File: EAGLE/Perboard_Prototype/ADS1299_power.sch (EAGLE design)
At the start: 24 parts

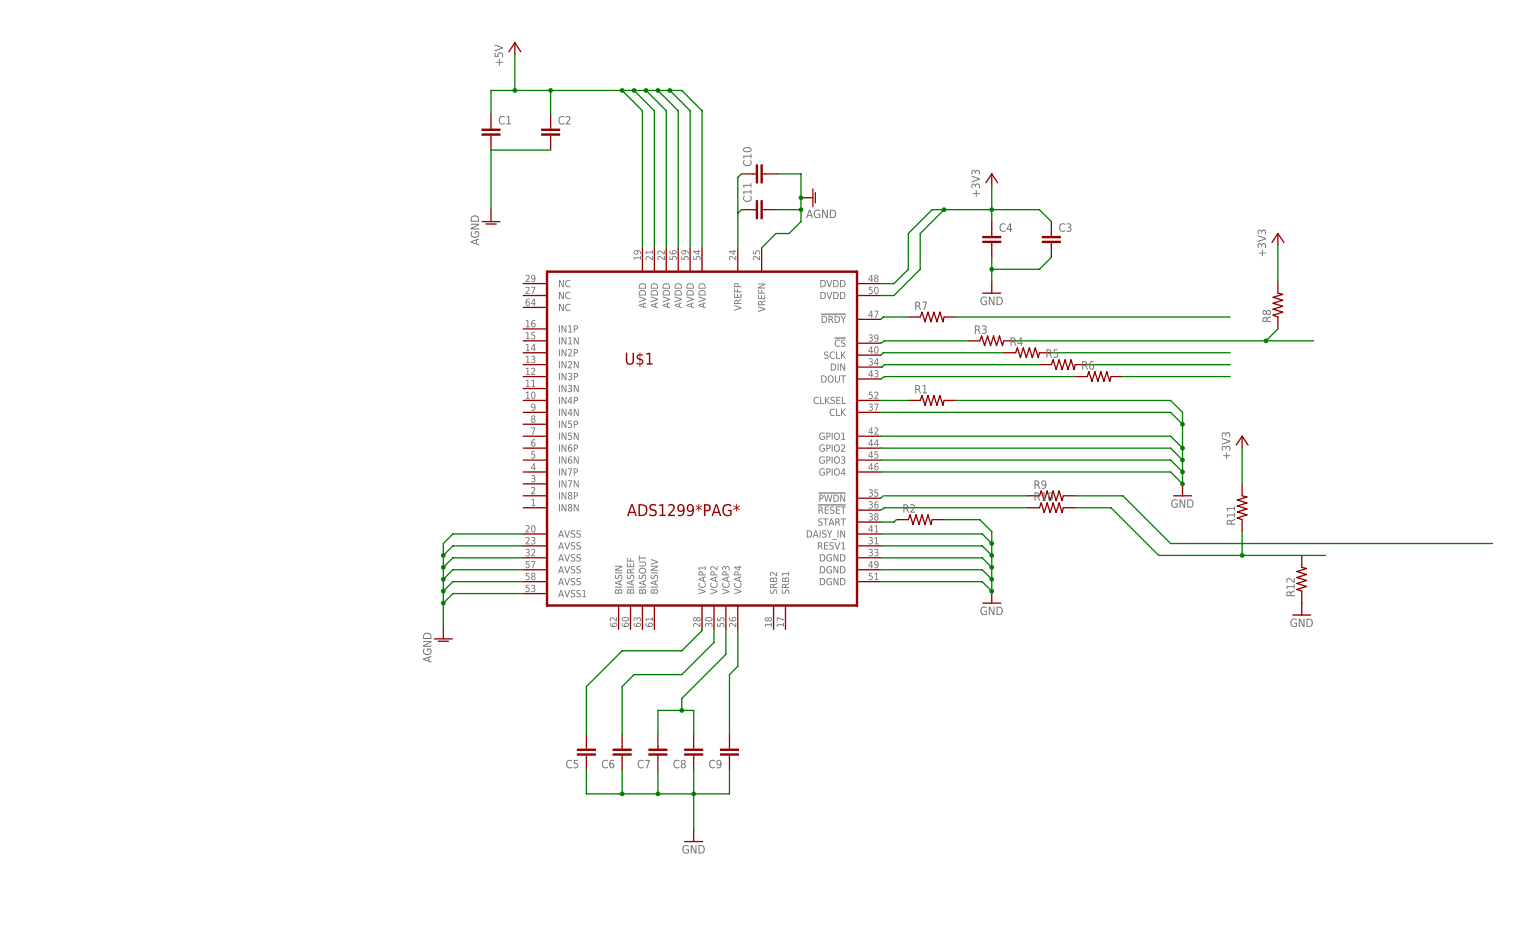
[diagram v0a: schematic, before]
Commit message: Completed design for Protoboard Wiring.
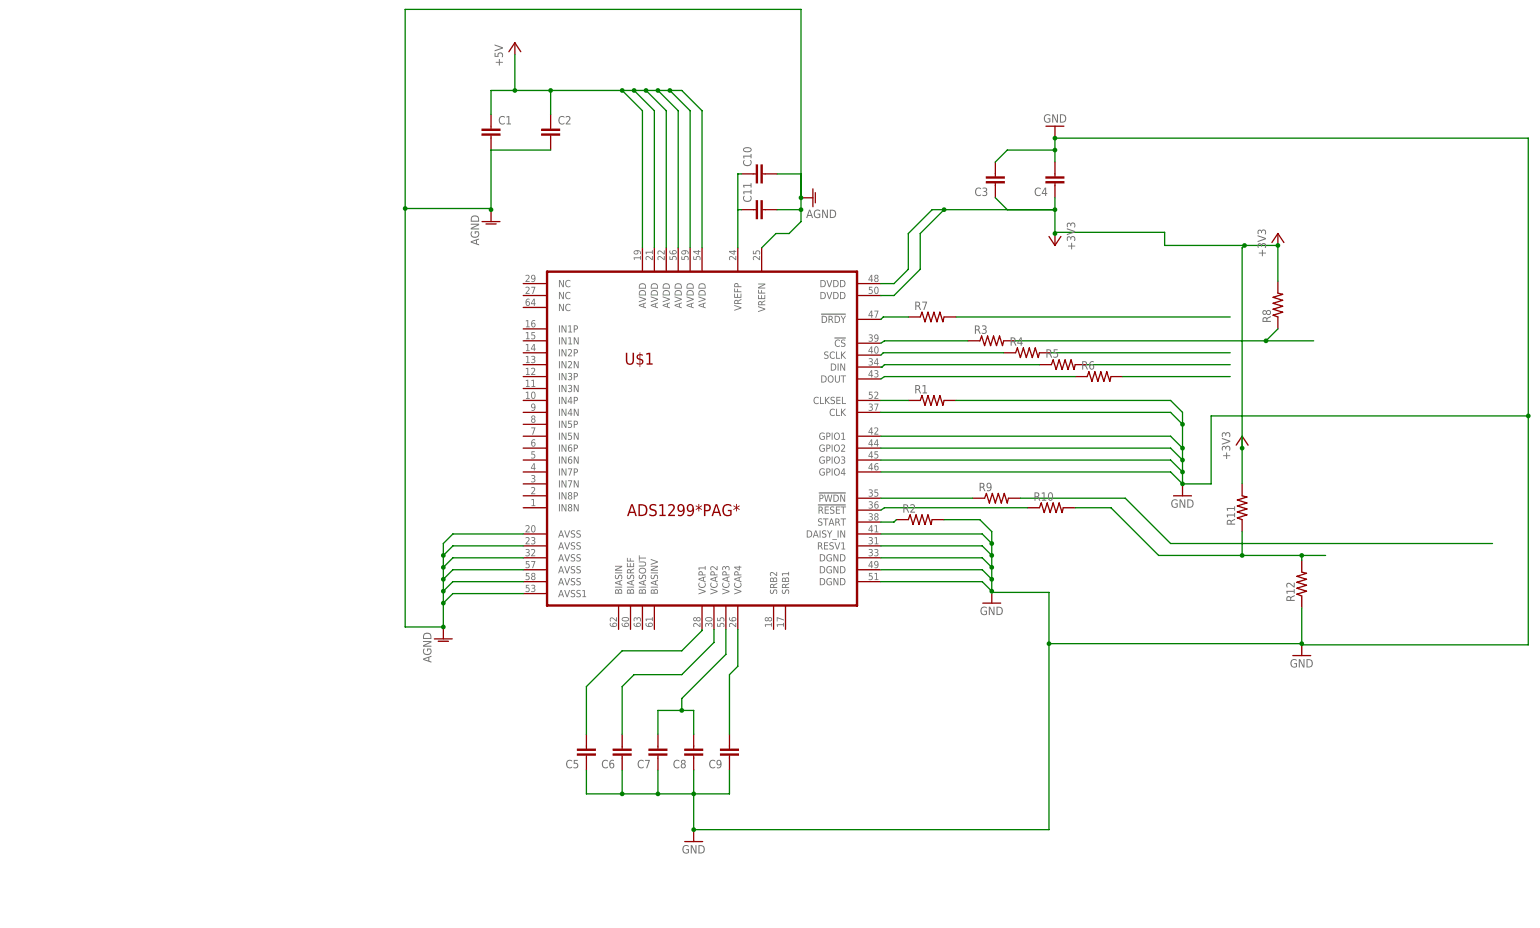
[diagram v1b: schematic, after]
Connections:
- removed net N$21 (its old number): R9.1
- net GND: now also R12.1
- net N$20: now also R9.1
- net N$22: now also R12.2
- net N$3: now also C11.1
- net N$7: now also R3.1
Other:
- moved on the sheet: C3, C4, R12, R9

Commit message: Re-routed all sides and placed components on top
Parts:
- C1, C4, C6, C7, C9: value (none) -> 1uF
- C10: value (none) -> 10uF
- C11, C2, C3, C8: value (none) -> 0.1uF
- C5: value (none) -> 100uF
- R1: value (none) -> 21K
- R12: value (none) -> 22k
- R2: value (none) -> 21k
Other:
- moved on the sheet: C11
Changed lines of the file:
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@@
 <parts>
 <part name="U$1" library="ADS129x" deviceset="ADS1299" device="*PAG*"/>
-<part name="C1" library="capacitor-wima" library_urn="urn:adsk.eagle:library:116" deviceset="C" device="2,5-3" package3d_urn="urn:adsk.eagle:package:5436/1"/>
-<part name="C2" library="capacitor-wima" library_urn="urn:adsk.eagle:library:116" deviceset="C" device="2,5-3" package3d_urn="urn:adsk.eagle:package:5436/1"/>
-<part name="C3" library="capacitor-wima" library_urn="urn:adsk.eagle:library:116" deviceset="C" device="2,5-3" package3d_urn="urn:adsk.eagle:package:5436/1"/>
-<part name="C4" library="capacitor-wima" library_urn="urn:adsk.eagle:library:116" deviceset="C" device="2,5-3" package3d_urn="urn:adsk.eagle:package:5436/1"/>
-<part name="C5" library="capacitor-wima" library_urn="urn:adsk.eagle:library:116" deviceset="C" device="2,5-3" package3d_urn="urn:adsk.eagle:package:5436/1"/>
-<part name="C6" library="capacitor-wima" library_urn="urn:adsk.eagle:library:116" deviceset="C" device="2,5-3" package3d_urn="urn:adsk.eagle:package:5436/1"/>
-<part name="C7" library="capacitor-wima" library_urn="urn:adsk.eagle:library:116" deviceset="C" device="2,5-3" package3d_urn="urn:adsk.eagle:package:5436/1"/>
-<part name="C8" library="capacitor-wima" library_urn="urn:adsk.eagle:library:116" deviceset="C" device="2,5-3" package3d_urn="urn:adsk.eagle:package:5436/1"/>
-<part name="C9" library="capacitor-wima" library_urn="urn:adsk.eagle:library:116" deviceset="C" device="2,5-3" package3d_urn="urn:adsk.eagle:package:5436/1"/>
-<part name="C10" library="capacitor-wima" library_urn="urn:adsk.eagle:library:116" deviceset="C" device="2,5-3" package3d_urn="urn:adsk.eagle:package:5436/1"/>
-<part name="C11" library="capacitor-wima" library_urn="urn:adsk.eagle:library:116" deviceset="C" device="2,5-3" package3d_urn="urn:adsk.eagle:package:5436/1"/>
+<part name="C1" library="capacitor-wima" library_urn="urn:adsk.eagle:library:116" deviceset="C" device="2,5-3" package3d_urn="urn:adsk.eagle:package:5436/1" value="1uF"/>
+<part name="C2" library="capacitor-wima" library_urn="urn:adsk.eagle:library:116" deviceset="C" device="2,5-3" package3d_urn="urn:adsk.eagle:package:5436/1" value="0.1uF"/>
+<part name="C3" library="capacitor-wima" library_urn="urn:adsk.eagle:library:116" deviceset="C" device="2,5-3" package3d_urn="urn:adsk.eagle:package:5436/1" value="0.1uF"/>
+<part name="C4" library="capacitor-wima" library_urn="urn:adsk.eagle:library:116" deviceset="C" device="2,5-3" package3d_urn="urn:adsk.eagle:package:5436/1" value="1uF"/>
+<part name="C5" library="capacitor-wima" library_urn="urn:adsk.eagle:library:116" deviceset="C" device="2,5-3" package3d_urn="urn:adsk.eagle:package:5436/1" value="100uF"/>
+<part name="C6" library="capacitor-wima" library_urn="urn:adsk.eagle:library:116" deviceset="C" device="2,5-3" package3d_urn="urn:adsk.eagle:package:5436/1" value="1uF"/>
+<part name="C7" library="capacitor-wima" library_urn="urn:adsk.eagle:library:116" deviceset="C" device="2,5-3" package3d_urn="urn:adsk.eagle:package:5436/1" value="1uF"/>
+<part name="C8" library="capacitor-wima" library_urn="urn:adsk.eagle:library:116" deviceset="C" device="2,5-3" package3d_urn="urn:adsk.eagle:package:5436/1" value="0.1uF"/>
+<part name="C9" library="capacitor-wima" library_urn="urn:adsk.eagle:library:116" deviceset="C" device="2,5-3" package3d_urn="urn:adsk.eagle:package:5436/1" value="1uF"/>
+<part name="C10" library="capacitor-wima" library_urn="urn:adsk.eagle:library:116" deviceset="C" device="2,5-3" package3d_urn="urn:adsk.eagle:package:5436/1" value="10uF"/>
+<part name="C11" library="capacitor-wima" library_urn="urn:adsk.eagle:library:116" deviceset="C" device="2,5-3" package3d_urn="urn:adsk.eagle:package:5436/1" value="0.1uF"/>
 <part name="GND2" library="supply1" library_urn="urn:adsk.eagle:library:371" deviceset="GND" device=""/>
 <part name="DGND" library="supply1" library_urn="urn:adsk.eagle:library:371" deviceset="GND" device=""/>
@@
 <part name="AGND3" library="supply1" library_urn="urn:adsk.eagle:library:371" deviceset="AGND" device=""/>
 <part name="DGND3" library="supply1" library_urn="urn:adsk.eagle:library:371" deviceset="GND" device=""/>
-<part name="R1" library="resistor" library_urn="urn:adsk.eagle:library:348" deviceset="R-US_" device="0204/2V" package3d_urn="urn:adsk.eagle:package:25948/1"/>
-<part name="R2" library="resistor" library_urn="urn:adsk.eagle:library:348" deviceset="R-US_" device="0204/2V" package3d_urn="urn:adsk.eagle:package:25948/1"/>
+<part name="R1" library="resistor" library_urn="urn:adsk.eagle:library:348" deviceset="R-US_" device="0204/2V" package3d_urn="urn:adsk.eagle:package:25948/1" value="21K"/>
+<part name="R2" library="resistor" library_urn="urn:adsk.eagle:library:348" deviceset="R-US_" device="0204/2V" package3d_urn="urn:adsk.eagle:package:25948/1" value="21k"/>
 <part name="R3" library="resistor" library_urn="urn:adsk.eagle:library:348" deviceset="R-US_" device="0204/2V" package3d_urn="urn:adsk.eagle:package:25948/1"/>
 <part name="R4" library="resistor" library_urn="urn:adsk.eagle:library:348" deviceset="R-US_" device="0204/2V" package3d_urn="urn:adsk.eagle:package:25948/1"/>
@@
 <part name="R11" library="resistor" library_urn="urn:adsk.eagle:library:348" deviceset="R-US_" device="0204/2V" package3d_urn="urn:adsk.eagle:package:25948/1"/>
 <part name="+3V3" library="supply1" library_urn="urn:adsk.eagle:library:371" deviceset="+3V3" device=""/>
-<part name="R12" library="resistor" library_urn="urn:adsk.eagle:library:348" deviceset="R-US_" device="0204/2V" package3d_urn="urn:adsk.eagle:package:25948/1"/>
+<part name="R12" library="resistor" library_urn="urn:adsk.eagle:library:348" deviceset="R-US_" device="0204/2V" package3d_urn="urn:adsk.eagle:package:25948/1" value="22k"/>
 <part name="DGND2" library="supply1" library_urn="urn:adsk.eagle:library:371" deviceset="GND" device=""/>
 </parts>
@@
 <instance part="C9" gate="G$1" x="60.96" y="-17.78" rot="R180"/>
 <instance part="C10" gate="G$1" x="66.04" y="106.68" rot="R90"/>
-<instance part="C11" gate="G$1" x="66.04" y="99.06" rot="R90"/>
+<instance part="C11" gate="G$1" x="66.04" y="96.52" rot="R90"/>
 <instance part="GND2" gate="1" x="130.302" y="116.84" rot="R180"/>
 <instance part="DGND" gate="1" x="116.84" y="15.24"/>
@@
 <wire x1="76.2" y1="106.68" x2="76.2" y2="101.6" width="0.1524" layer="91"/>
 <pinref part="C11" gate="G$1" pin="2"/>
-<wire x1="71.12" y1="99.06" x2="76.2" y2="99.06" width="0.1524" layer="91"/>
+<wire x1="71.12" y1="96.52" x2="76.2" y2="99.06" width="0.1524" layer="91"/>
 <wire x1="76.2" y1="99.06" x2="76.2" y2="101.6" width="0.1524" layer="91"/>
 <junction x="76.2" y="101.6"/>
@@
 <pinref part="C11" gate="G$1" pin="1"/>
 <wire x1="62.738" y1="90.932" x2="62.738" y2="99.06" width="0.1524" layer="91"/>
-<wire x1="63.5" y1="99.06" x2="62.738" y2="99.06" width="0.1524" layer="91"/>
+<wire x1="63.5" y1="96.52" x2="62.738" y2="99.06" width="0.1524" layer="91"/>
 <wire x1="62.738" y1="99.06" x2="62.738" y2="106.68" width="0.1524" layer="91"/>
 <pinref part="C10" gate="G$1" pin="1"/>

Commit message: updated schematic and board
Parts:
- R2: value 21k -> 22k
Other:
- moved on the sheet: C1, C10, C11, C2, C3, C4, C5, C6, C7, C8, C9, R1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
